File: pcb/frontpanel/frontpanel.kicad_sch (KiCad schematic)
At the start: 1 part

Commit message: Continued work on front panel
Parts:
- added C? (x2): 4.7 uF, symbol device:C
- added C? (x6): 0.47 uF, azonenberg_pcb:EIA_0402_CAP_NOSILK, symbol device:C
- added C?: 0.1 uF, azonenberg_pcb:EIA_0402_CAP_NOSILK, symbol device:C
- added C?: 4.7 uF, azonenberg_pcb:EIA_0603_CAP_NOSILK, symbol device:C
- added D? (x32): GREEN, symbol device:LED
- added FB?: MI0603J601R-10, azonenberg_pcb:EIA_0603_INDUCTOR_NOSILK, symbol passive-azonenberg:INDUCTOR_PWROUT
- added J?: CONN_01X05, azonenberg_pcb:CONN_HEADER_2.54MM_1x5, symbol conn:CONN_01X05
- added J?, TP?: CONN_01X03, azonenberg_pcb:CONN_HEADER_2.54MM_1x3, symbol conn:CONN_01X03
- added R?: 10K, symbol device:R
- added R? (x32): 470, symbol device:R
- added R? (x2): 4.7K, symbol device:R
- added R?: 10K, azonenberg_pcb:EIA_0402_RES_NOSILK, symbol device:R
- added R?: DNP, azonenberg_pcb:EIA_0402_RES_NOSILK, symbol device:R
- added U? (x3): STM32L031-QFN32, symbol st-azonenberg:STM32L031-QFN32
- added U?: TCA6424A, symbol special-azonenberg:TCA6424A
- added U?: STM32L031C6U6, azonenberg_pcb:QFN_48_0.5MM_7x7MM, symbol st-azonenberg:STM32L031-UFQFPN48
- added U?: LTC3122, symbol power-azonenberg:LTC3122
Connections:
- net 3V3: now also C?.1, C?.1, U?.27 (VCCP)
- net 3V3_SB: now also C?.1, C?.1, C?.1, C?.1, C?.1, C?.1, FB?.2, J?.1 (P1), R?.1, R?.1, R?.1, U?.24 (VDD), U?.31 (VCCI), U?.36 (VDD), U?.48 (VDD)
- net FRONTPANEL_CS_N: now also U?.10 (PA4)
- net FRONTPANEL_MISO: now also U?.12 (PA6)
- net FRONTPANEL_MOSI: now also U?.13 (PA7)
- net FRONTPANEL_SCK: now also U?.11 (PA5)
- net GND: now also C?.2, C?.2, C?.2, C?.2, C?.2, C?.2, C?.2, C?.2, C?.2, C?.2, D?.1 (K), D?.1 (K), D?.1 (K), D?.1 (K), D?.1 (K), D?.1 (K), D?.1 (K), D?.1 (K), D?.1 (K), D?.1 (K), D?.1 (K), D?.1 (K), D?.1 (K), D?.1 (K), D?.1 (K), D?.1 (K), D?.1 (K), D?.1 (K), D?.1 (K), D?.1 (K), D?.1 (K), D?.1 (K), D?.1 (K), D?.1 (K), D?.1 (K), D?.1 (K), D?.1 (K), D?.1 (K), D?.1 (K), D?.1 (K), D?.1 (K), D?.1 (K), J?.2 (P2), J?.3 (P3), R?.2, R?.2, TP?.3 (P3), U?.10 (SGND), U?.2 (PGND), U?.23 (VSS), U?.25 (GND), U?.26 (ADDR), U?.35 (VSS), U?.47 (VSS), U?.8 (VSSA), U?.PAD (GND), U?.PAD (VSS)
- new net: D?.2 (A), R?.2 (x32)
- new net 12V0_EN: R?.1, U?.6 (PA0)
- new net A3V3: C?.1, FB?.1, U?.9 (VDDA)
- new net BOOT0: R?.1, U?.44 (BOOT0)
- new net DIRIN_LED_0: R?.1, U?.25 (PA15)
- new net DIRIN_LED_1: R?.1, U?.27 (PB4)
- new net DIRIN_LED_2: R?.1, U?.28 (PB5)
- new net DIRIN_LED_3: R?.1, U?.32 (PB8)
- new net DIROUT_LED_0: R?.1, U?.14 (PB0)
- new net DIROUT_LED_1: R?.1, U?.15 (PB1)
- new net DIROUT_LED_2: R?.1, U?.16 (PB2)
- new net DIROUT_LED_3: R?.1, U?.26 (PB3)
- new net I2C_SCL: R?.2, TP?.1 (P1), U?.19 (PA9), U?.29 (SCL)
- new net I2C_SDA: R?.2, TP?.2 (P2), U?.20 (PA10), U?.30 (SDA)
- new net RST_N: C?.1, J?.5 (P5), R?.2, U?.7 (NRST)
- new net SWCLK: J?.3 (P3), U?.24 (PA14)
- new net SWDIO: J?.4 (P4), U?.23 (PA13)
- new net TCA_RST_N: U?.28 (RESET_N), U?.7 (PA1)
- new net TRIGIN_LED_0: R?.1, U?.1 (P00)
- new net TRIGIN_LED_1: R?.1, U?.2 (P01)
- new net TRIGIN_LED_10: R?.1, U?.11 (P12)
- new net TRIGIN_LED_11: R?.1, U?.12 (P13)
- new net TRIGIN_LED_2: R?.1, U?.3 (P02)
- new net TRIGIN_LED_3: R?.1, U?.4 (P03)
- new net TRIGIN_LED_4: R?.1, U?.5 (P04)
- new net TRIGIN_LED_5: R?.1, U?.6 (P05)
- new net TRIGIN_LED_6: R?.1, U?.7 (P06)
- new net TRIGIN_LED_7: R?.1, U?.8 (P07)
- new net TRIGIN_LED_8: R?.1, U?.9 (P10)
- new net TRIGIN_LED_9: R?.1, U?.10 (P11)
- new net TRIGOUT_LED_0: R?.1, U?.13 (P14)
- new net TRIGOUT_LED_1: R?.1, U?.14 (P15)
- new net TRIGOUT_LED_10: R?.1, U?.23 (P26)
- new net TRIGOUT_LED_11: R?.1, U?.24 (P27)
- new net TRIGOUT_LED_2: R?.1, U?.15 (P16)
- new net TRIGOUT_LED_3: R?.1, U?.16 (P17)
- new net TRIGOUT_LED_4: R?.1, U?.17 (P20)
- new net TRIGOUT_LED_5: R?.1, U?.18 (P21)
- new net TRIGOUT_LED_6: R?.1, U?.19 (P22)
- new net TRIGOUT_LED_7: R?.1, U?.20 (P23)
- new net TRIGOUT_LED_8: R?.1, U?.21 (P24)
- new net TRIGOUT_LED_9: R?.1, U?.22 (P25)
- new net UART_RX: J?.1 (P1), U?.30 (PB7)
- new net UART_TX: J?.2 (P2), U?.29 (PB6)
- no-connect marks 0 -> 8
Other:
- note added: "I2C ADDRESS MAP * LCD = 0x78 * IO expander = 0x44 (ADDR=0)"
- note added: "no need for debug connector on SPI bus host board has one already"

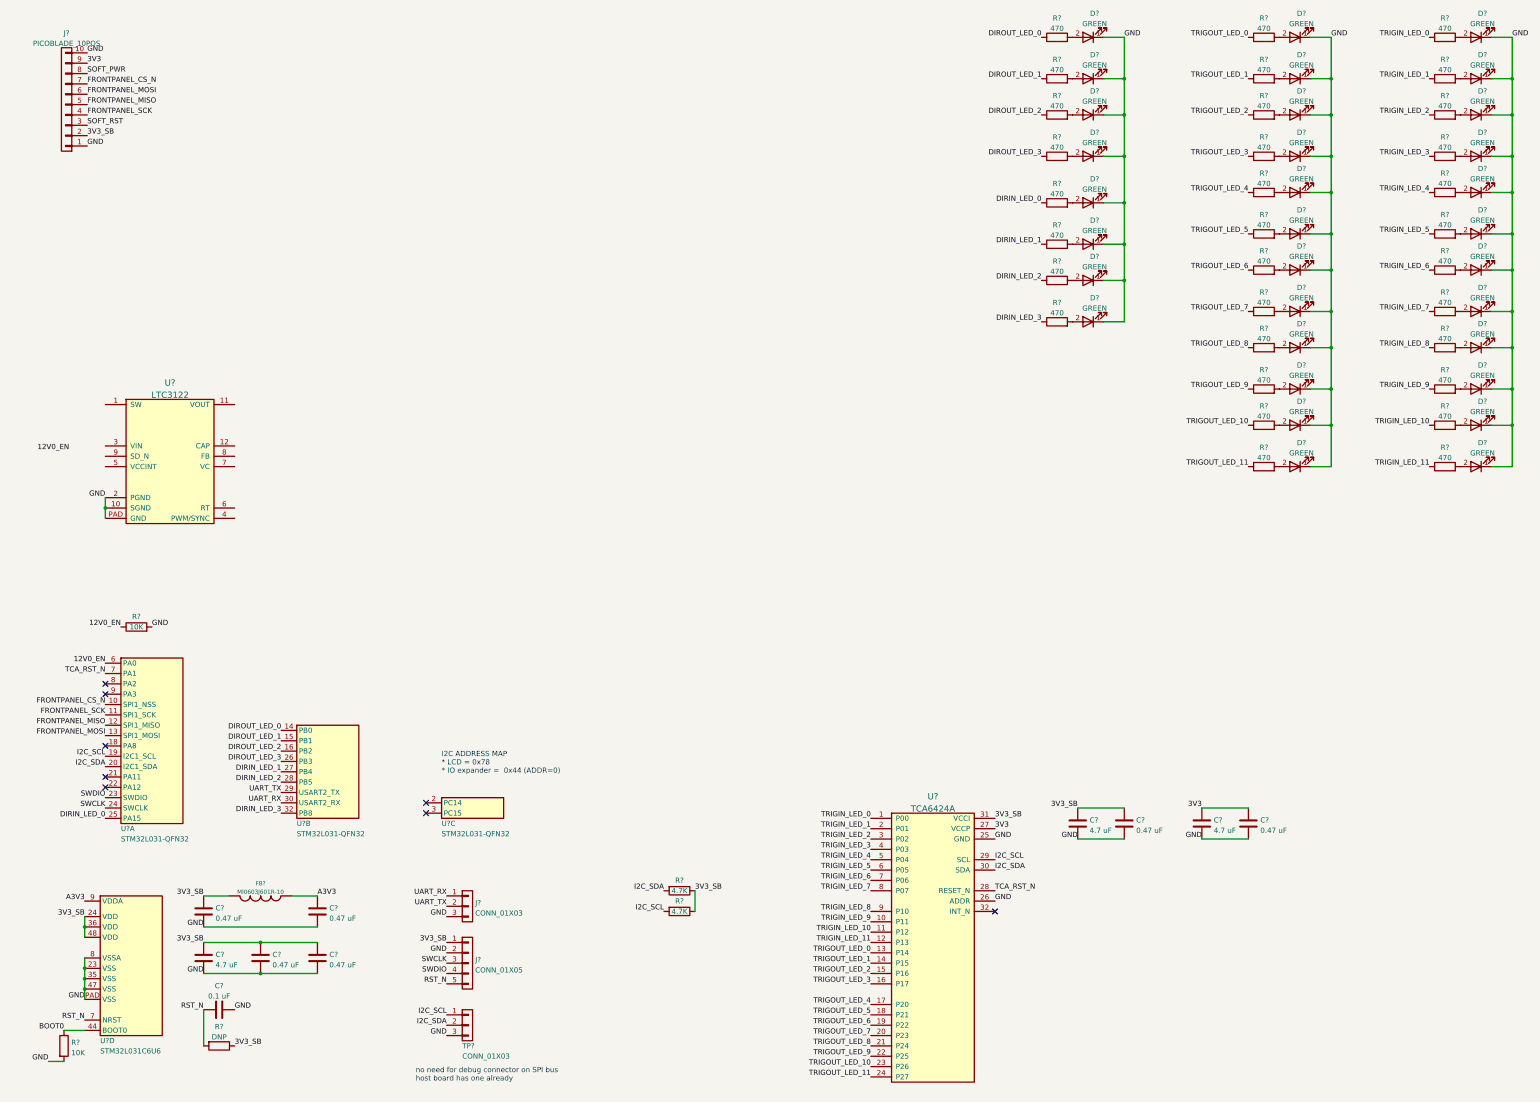
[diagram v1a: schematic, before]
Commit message: Updated front panel sch to use STM32L431 with more SRAM and SPI interfaces
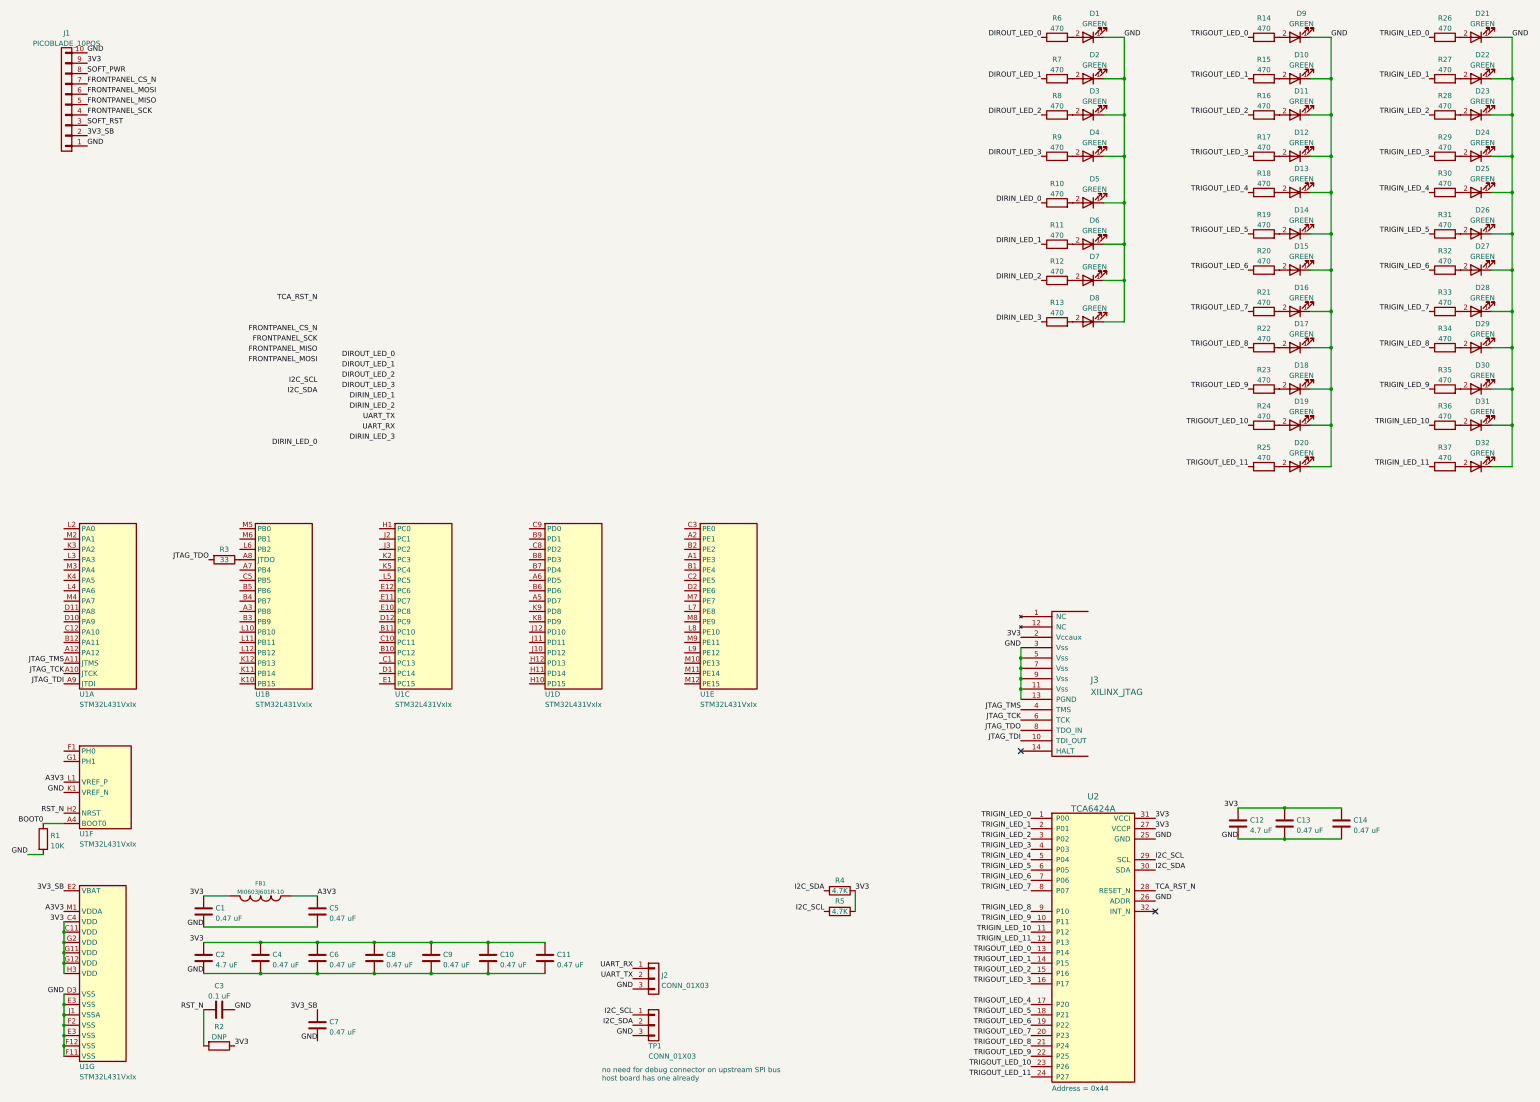
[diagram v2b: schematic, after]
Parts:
- removed C?: 4.7 uF, symbol device:C
- removed J?: CONN_01X05, azonenberg_pcb:CONN_HEADER_2.54MM_1x5, symbol conn:CONN_01X05
- removed R?: 10K, symbol device:R
- removed U? (x3): STM32L031-QFN32, symbol st-azonenberg:STM32L031-QFN32
- removed U?: STM32L031C6U6, azonenberg_pcb:QFN_48_0.5MM_7x7MM, symbol st-azonenberg:STM32L031-UFQFPN48
- removed U?: LTC3122, symbol power-azonenberg:LTC3122
- added C10, C11, C7, C8, C9: 0.47 uF, azonenberg_pcb:EIA_0402_CAP_NOSILK, symbol device:C
- added J3: XILINX_JTAG, azonenberg_pcb:XILINX_JTAG_PTH_MOLEX_0878311420, symbol xilinx-azonenberg:XILINX_JTAG
- added R3: 33, azonenberg_pcb:EIA_0402_RES_NOSILK, symbol device:R
- added U1: STM32L431VxIx, azonenberg_pcb:BGA_100_7x7_DEPOP_0.5MM_STM32_UFBGA100_OSHPARK, symbol st-azonenberg:STM32L431VxIx
- C12: renamed from C?; footprint (none) -> azonenberg_pcb:EIA_0603_CAP_NOSILK
- D1, D10, D11, D12, D13, D14, D15, D16, D17, D18, D19, D2, D20, D21, D22, D23, D24, D25, D26, D27, D28, D29, D3, D30, D31, D32, D4, D5, D6, D7, D8, D9: renamed from D?; footprint (none) -> azonenberg_pcb:EIA_0603_LED
- R10, R11, R12, R13, R14, R15, R16, R17, R18, R19, R20, R21, R22, R23, R24, R25, R26, R27, R28, R29, R30, R31, R32, R33, R34, R35, R36, R37, R4, R5, R6, R7, R8, R9: renamed from R?; footprint (none) -> azonenberg_pcb:EIA_0402_RES_NOSILK
- U2: renamed from U?; footprint (none) -> azonenberg_pcb:QFN_32_0.5MM_5x5MM
- gave numbers to parts that had none: 14
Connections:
- net 3V3: now also C1.1, C12.1, C13.1, C2.1, C4.1, C6.1, FB1.2, R2.1, R4.1, R5.1, U2.31 (VCCI), C10.1, C11.1, C8.1, C9.1, J3.2 (Vccaux), U1.C11 (VDD), U1.C4 (VDD), U1.G11 (VDD), U1.G12 (VDD), U1.G2 (VDD), U1.H3 (VDD)
- net 3V3_SB: now also C7.1, U1.E2 (VBAT); no longer C1.1, C12.1, C13.1, C2.1, C4.1, C6.1, FB1.2, R2.1, R4.1, R5.1, U2.31 (VCCI)
- net A3V3: now also U1.L1 (VREF_P), U1.M1 (VDDA)
- net BOOT0: now also U1.A4 (BOOT0)
- net GND: now also C10.2, C11.2, C7.2, C8.2, C9.2, J3.11 (Vss), J3.13 (PGND), J3.3 (Vss), J3.5 (Vss), J3.7 (Vss), J3.9 (Vss), U1.D3 (VSS), U1.E3 (VSS), U1.F11 (VSS), U1.F12 (VSS), U1.F2 (VSS), U1.J1 (VSSA), U1.K1 (VREF_N)
- net RST_N: now also U1.H2 (NRST)
- new net: R3.1, U1.A8 (PB3)
- new net JTAG_TCK: J3.6 (TCK), U1.A10 (PA14)
- new net JTAG_TDI: J3.10 (TDI_OUT), U1.A9 (PA15)
- new net JTAG_TDO: J3.8 (TDO_IN), R3.2
- new net JTAG_TMS: J3.4 (TMS), U1.A11 (PA13)
- no-connect marks 8 -> 2
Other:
- note added: "Address = 0x44"
- note added: "no need for debug connector on upstream SPI bus host board has one already"
- note removed: "I2C ADDRESS MAP * LCD = 0x78 * IO expander = 0x44 (ADDR=0)"
- note removed: "no need for debug connector on SPI bus host board has one already"
- moved on the sheet: C12, C13, C14, J2, R1, R4, R5, TP1, U2

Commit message: Finished initial front panel schematic and design review
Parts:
- added C15: 4.7 uF, azonenberg_pcb:EIA_0603_CAP_NOSILK, symbol device:C
- added C16, C17, C26: 0.47 uF, azonenberg_pcb:EIA_0402_CAP_NOSILK, symbol device:C
- added C18: 4.7 uF 25V, azonenberg_pcb:EIA_0805_CAP_NOSILK, symbol device:C
- added C19, C20, C21, C22, C23, C24, C25: 1 uF 25V, azonenberg_pcb:EIA_0805_CAP_NOSILK, symbol device:C
- added D33, D34, D35: CTS05S30,L3F, azonenberg_pcb:SOD882, symbol device:D_Schottky
- added J4: DISPLAY, azonenberg_pcb:CONN_FFC_0.5MM_1x24_HIROSE_FH34SRJ-24S-0.5SH(50), symbol conn:CONN_01X24
- added L1: TFM322512ALMA100MTAA, azonenberg_pcb:EIA_1210_CAP_NOSILK, symbol passive-azonenberg:INDUCTOR_PWROUT
- added M1: LOGO, azonenberg_pcb:LONGTHING-1200DPI, symbol special-azonenberg:MECHANICAL
- added M2: LOGO, w_logo:Logo_silk_WEEE_3.4x5mm, symbol special-azonenberg:MECHANICAL
- added M3: LOGO, w_logo:Logo_silk_OSHW_6x6mm, symbol special-azonenberg:MECHANICAL
- added M4: LOGO, w_logo:Logo_silk_ROHS_10x5.6mm, symbol special-azonenberg:MECHANICAL
- added MH1, MH2, MH3, MH4: SCREWHOLE, azonenberg_pcb:MECHANICAL_CLEARANCEHOLE_4_40, symbol conn:CONN_01X01
- added Q1: SSM6N58NU, azonenberg_pcb:DFN_6_0.65MM_2x2MM_GDS, symbol special-azonenberg:SSM6N58NU_DUAL_NMOS
- added R38: 0.47, azonenberg_pcb:EIA_0402_RES_NOSILK, symbol device:R
- added SW1, SW2: SWITCH, azonenberg_pcb:SWITCH_RAFI_MICON_5, symbol passive-azonenberg:SWITCH
- added TP2, TP3: CONN_01X08, azonenberg_pcb:CONN_HEADER_2.54MM_1x8, symbol conn:CONN_01X08
- added TP4, TP5: U.FL, azonenberg_pcb:CONN_U.FL_TE_1909763-1, symbol conn:CONN_COAXIAL
- added U3: AT30TS74_UDFN, azonenberg_pcb:DFN_8_0.5MM_2x3MM_TALL, symbol special-azonenberg:AT30TS74_UDFN
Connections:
- net 3V3: now also C15.1, C16.1, C17.1, C26.1, J4.15 (P15), J4.16 (P16), L1.2, TP4.1 (In), U3.8 (VCC)
- net 3V3_SB: now also SW1.2, SW2.2, TP5.1 (In)
- net DIRIN_LED_0: now also U1.M9 (PE11)
- net DIRIN_LED_1: now also U1.M11 (PE14)
- net DIRIN_LED_2: now also U1.A2 (PE1)
- net DIRIN_LED_3: now also U1.A1 (PE3)
- net DIROUT_LED_0: now also U1.D12 (PC9)
- net DIROUT_LED_1: now also U1.E12 (PC6)
- net DIROUT_LED_2: now also U1.J12 (PD10)
- net DIROUT_LED_3: now also U1.H12 (PD13)
- net FRONTPANEL_CS_N: now also U1.M5 (PB0)
- net FRONTPANEL_MISO: now also U1.A7 (PB4)
- net FRONTPANEL_MOSI: now also U1.M12 (PE15)
- net FRONTPANEL_SCK: now also U1.M10 (PE13)
- net GND: now also C15.2, C16.2, C17.2, C19.2, C20.2, C21.2, C23.2, C26.2, D33.1 (K), J4.17 (P17), Q1.D2 (D), Q1.G2 (G), Q1.S2 (S), R38.2, TP2.8 (P8), TP3.8 (P8), TP4.2 (Ext), TP5.2 (Ext), U3.4 (GND), U3.5 (A2), U3.6 (A1), U3.7 (A0); no longer J3.13 (PGND)
- net I2C_SCL: now also U1.K12 (PB13), U3.2 (SCL)
- net I2C_SDA: now also U1.L11 (PB11), U3.1 (SDA)
- net SOFT_PWR: now also SW1.1
- net SOFT_RST: now also SW2.1
- net TCA_RST_N: now also U1.M8 (PE9)
- net UART_RX: now also U1.B6 (PD6)
- net UART_TX: now also U1.A6 (PD5)
- net DPY_RST_N: now reaches U1.M6 (PB1)
- net DPY_RST_N: now also J4.10 (P10), TP2.4 (P4), TP3.4 (P4)
- net DPY_DC: now reaches U1.M7 (PE7)
- net DPY_DC: now also J4.11 (P11), TP2.1 (P1), TP3.3 (P3)
- net DPY_SPI_DATA: now reaches U1.B10 (PC12)
- net DPY_SPI_DATA: now also J4.14 (P14), TP2.3 (P3), TP3.7 (P7)
- net DPY_SPI_SCK: now reaches U1.B11 (PC10)
- net DPY_SPI_SCK: now also J4.13 (P13), TP2.2 (P2), TP3.6 (P6)
- net DPY_BS: now reaches U1.M2 (PA1)
- net DPY_BS: now also J4.8 (P8), TP2.5 (P5), TP3.2 (P2)
- net DPY_SPI_CS_N: now reaches U1.M3 (PA4)
- net DPY_SPI_CS_N: now also J4.12 (P12), TP2.6 (P6), TP3.5 (P5)
- net DPY_BUSY_N: now reaches U1.M4 (PA7)
- net DPY_BUSY_N: now also J4.9 (P9), TP2.7 (P7), TP3.1 (P1)
- new net: C18.2, D33.2 (A), D34.1 (K)
- new net: C18.1, D35.2 (A), L1.1, Q1.D1 (D)
- new net: C22.2, C24.2, C25.2
- new net DPY_GDR: J4.2 (P2), Q1.G1 (G)
- new net DPY_RESE: J4.3 (P3), Q1.S1 (S), R38.1
- new net DPY_VCOM: C24.1, J4.24 (P24)
- new net DPY_VDDD: C23.1, J4.18 (P18)
- new net DPY_VDH: C22.1, J4.20 (P20)
- new net DPY_VDL: C25.1, J4.22 (P22)
- new net DPY_VGH: C20.1, D35.1 (K), J4.21 (P21)
- new net DPY_VGL: C19.1, D34.2 (A), J4.23 (P23)
- new net DPY_VHDR: C21.1, J4.5 (P5)
- no-connect marks 2 -> 67
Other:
- note added: "Address = 0x90"
